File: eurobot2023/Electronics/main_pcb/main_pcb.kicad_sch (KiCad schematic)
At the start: 4 parts, among them J1 PI40HAT, J2 Conn_01x03, Q1 BSH108,215, U1 PCA9517AD

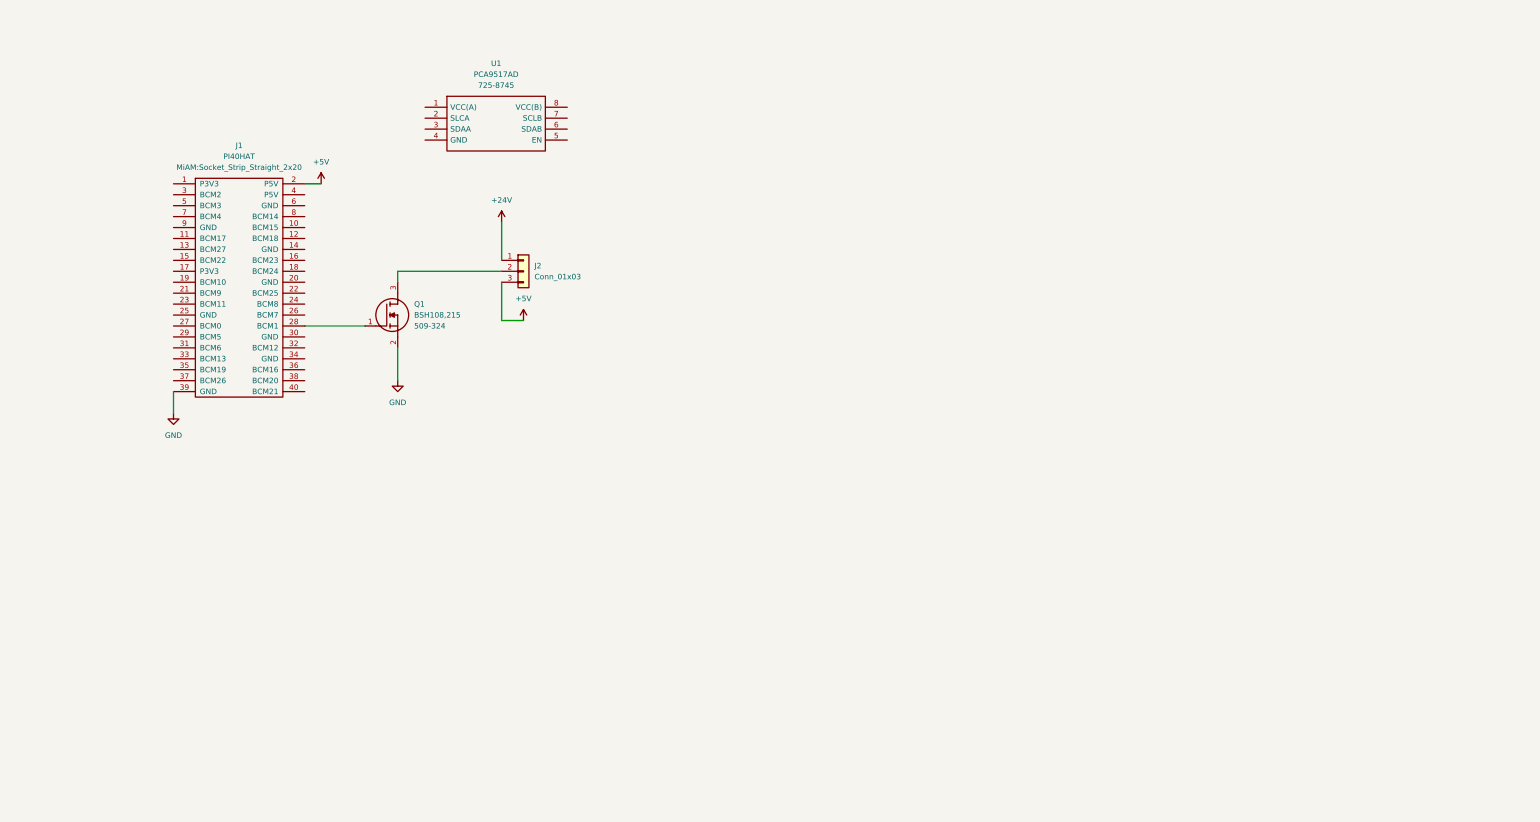
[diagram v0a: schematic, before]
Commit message: Electronics: partial draft of PCB.
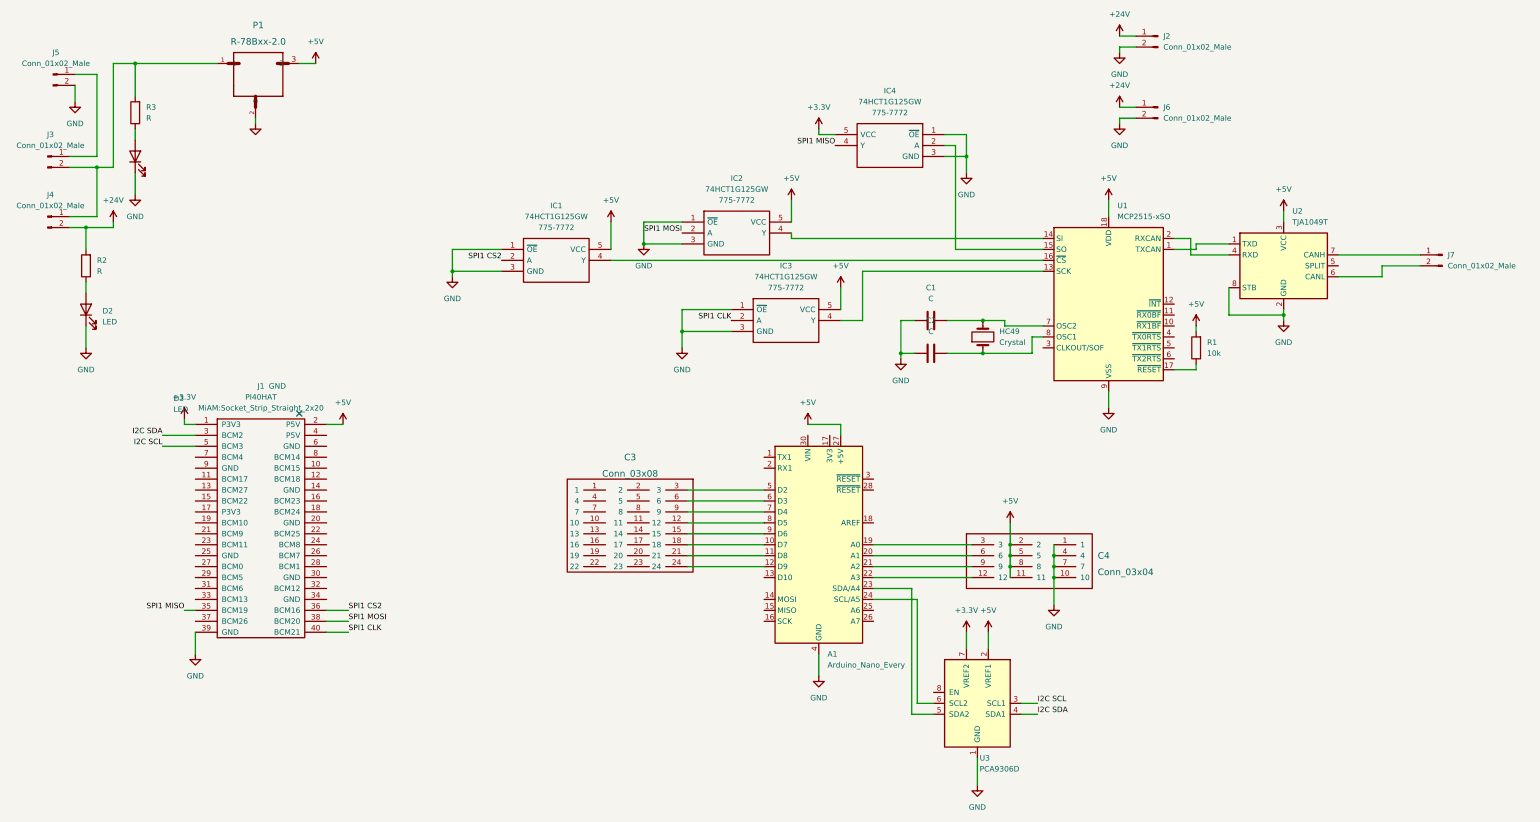
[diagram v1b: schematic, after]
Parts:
- removed J2: Conn_01x03, symbol Connector_Generic:Conn_01x03
- removed Q1: BSH108,215, SOT95P230X110-3N, symbol MiAM:BSH108,215
- removed U1: PCA9517AD, SOIC127P600X175-8N, symbol MiAM:PCA9517AD
- added A1: Arduino_Nano_Every, Module:Arduino_Nano, symbol MCU_Module:Arduino_Nano_Every
- added C1, C2: C, Capacitor_THT:C_Rect_L10.0mm_W2.5mm_P7.50mm_MKS4, symbol Device:C
- added C3: Conn_03x08, MiAM:Pin_Header_Straight_3x08_Pitch2.54mm, symbol MiAM:Conn_03x08
- added C4: Conn_03x04, MiAM:Pin_Header_Straight_3x04_Pitch2.54mm, symbol MiAM:Conn_03x04
- added D2, D3: LED, LED_THT:LED_D3.0mm, symbol Device:LED
- added HC49: Crystal, Crystal:Crystal_HC49-4H_Vertical, symbol Device:Crystal
- added IC1, IC2, IC3, IC4: 74HCT1G125GW, SOT65P210X110-5N, symbol MiAM:74HCT1G125GW
- added J2, J3, J4, J5, J6: Conn_01x02_Male, MiAM:XT30PWF, symbol Connector:Conn_01x02_Male
- added J7: Conn_01x02_Male, Connector_PinHeader_2.54mm:PinHeader_1x02_P2.54mm_Vertical, symbol Connector:Conn_01x02_Male
- added P1: R-78Bxx-2.0, MiAM:CONV_R-78Bxx-2.0, symbol MiAM:R-78Bxx-2.0
- added R1: 10k, Resistor_THT:R_Axial_DIN0309_L9.0mm_D3.2mm_P12.70mm_Horizontal, symbol Device:R
- added R2, R3: R, Resistor_THT:R_Axial_DIN0309_L9.0mm_D3.2mm_P12.70mm_Horizontal, symbol Device:R
- added U1: MCP2515-xSO, Package_SO:SOIC-18W_7.5x11.6mm_P1.27mm, symbol Interface_CAN_LIN:MCP2515-xSO
- added U2: TJA1049T, Package_SO:SOIC-8_3.9x4.9mm_P1.27mm, symbol Interface_CAN_LIN:TJA1049T
- added U3: PCA9306D, Package_SO:SO-8_3.9x4.9mm_P1.27mm, symbol Interface:PCA9306D
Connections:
- net +24V: now also J2.1 (Pin_1), J4.2 (Pin_2), J6.1 (Pin_1), R2.2
- net +5V: now also A1.27 (+5V), C4.11, C4.2, C4.5, C4.8, IC1.5 (VCC), IC2.5 (VCC), IC3.5 (VCC), P1.3, R1.2, U1.18 (VDD), U2.3 (VCC), U3.2 (VREF1)
- net GND: now also A1.29 (GND), A1.4 (GND), C1.1, C2.1, C4.1, C4.10, C4.4, C4.7, D2.1 (K), D3.1 (K), IC1.1 (~{OE}), IC1.3 (GND), IC2.1 (~{OE}), IC2.3 (GND), IC3.1 (~{OE}), IC3.3 (GND), IC4.1 (~{OE}), IC4.3 (GND), J2.2 (Pin_2), J5.2 (Pin_2), J6.2 (Pin_2), P1.2, U1.9 (VSS), U2.2 (GND), U2.8 (STB), U3.1 (GND)
- net +3.3V: now reaches J1.1 (P3V3)
- net +3.3V: now also IC4.5 (VCC), U3.7 (VREF2)
- net I2C SDA: now reaches J1.3 (BCM2)
- net I2C SDA: now also U3.4 (SDA1)
- net SPI1 MISO: now reaches J1.35 (BCM19)
- net SPI1 MISO: now also IC4.4 (Y)
- net SPI1 CS2: now reaches J1.36 (BCM16)
- net SPI1 CS2: now also IC1.2 (A)
- net SPI1 MOSI: now reaches J1.38 (BCM20)
- net SPI1 MOSI: now also IC2.2 (A)
- net SPI1 CLK: now reaches J1.40 (BCM21)
- net SPI1 CLK: now also IC3.2 (A)
- net I2C SCL: now reaches J1.5 (BCM3)
- net I2C SCL: now also U3.3 (SCL1)
- new net: J3.1 (Pin_1), J5.1 (Pin_1)
- new net: A1.22 (A3), C4.12
- new net: A1.19 (A0), C4.3
- new net: A1.20 (A1), C4.6
- new net: A1.21 (A2), C4.9
- new net: IC3.4 (Y), U1.13 (SCK)
- new net: J3.2 (Pin_2), J4.1 (Pin_1), P1.1, R3.2
- new net: IC2.4 (Y), U1.14 (SI)
- new net: U1.1 (TXCAN), U2.1 (TXD)
- new net: U1.2 (RXCAN), U2.4 (RXD)
- new net: J7.2 (Pin_2), U2.6 (CANL)
- new net: J7.1 (Pin_1), U2.7 (CANH)
- new net: A1.10 (D7), C3.18
- new net: A1.11 (D8), C3.21
- new net: A1.12 (D9), C3.24
- new net: A1.23 (SDA/A4), U3.5 (SDA2)
- new net: A1.24 (SCL/A5), U3.6 (SCL2)
- new net: A1.5 (D2), C3.3
- new net: A1.6 (D3), C3.6
- new net: A1.7 (D4), C3.9
- new net: A1.8 (D5), C3.12
- new net: A1.9 (D6), C3.15
- new net: IC4.2 (A), U1.15 (SO)
- new net: C2.2, HC49.1, U1.8 (OSC1)
- new net: C1.2, HC49.2, U1.7 (OSC2)
- new net: D2.2 (A), R2.1
- new net: IC1.4 (Y), U1.16 (~{CS})
- new net: D3.2 (A), R3.1
- new net: R1.1, U1.17 (~{RESET})
- no-connect marks 0 -> 1
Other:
- moved on the sheet: J1

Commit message: [eurobot2023/Electronics] Continue schematic
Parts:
- removed IC1, IC2, IC4: 74HCT1G125GW, SOT65P210X110-5N, symbol MiAM:74HCT1G125GW
- added IC1: 74HCT541D,652, SOIC127P1032X265-20N, symbol MiAM:74HCT541D,652
- added IC2: SN74LVC126ADR, SOIC127P600X175-14N, symbol MiAM:SN74LVC126ADR
- added J10: Conn_01x02_Male, Connector_PinHeader_2.54mm:PinHeader_1x02_P2.54mm_Vertical, symbol Connector:Conn_01x02_Male
- added J8: Conn_01x03_Male, Connector_PinHeader_2.54mm:PinHeader_1x03_P2.54mm_Vertical, symbol Connector:Conn_01x03_Male
- added J9: 22-03-5035, SHDR3W60P0X250_1X3_990X490X590P, symbol MiAM:22-03-5035
- added R4, R5, R6: 10k, Resistor_THT:R_Axial_DIN0309_L9.0mm_D3.2mm_P12.70mm_Horizontal, symbol Device:R
- added U4: Pololu_MAX14870, MiAM:PololuMAX14870, symbol MiAM:Pololu_MAX14870
- J1: footprint MiAM:Socket_Strip_Straight_2x20 -> MiAM:MODULE_RASPBERRY_PI_B+
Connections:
- net +24V: now also J8.3 (Pin_3)
- net +3.3V: now also IC2.1 (1OE), IC2.10 (3OE), IC2.13 (4OE), IC2.14 (VCC), R4.2, R5.2
- net +5V: now also J1.4 (P5V), IC1.20 (VCC), R6.2
- net GND: now also IC1.1 (~{OE1}), IC1.10 (GND), IC1.19 (~{OE2}), IC2.7 (GND), J9.3, U4.4 (nEnable), U4.5 (GND); no longer IC3.1 (~{OE})
- net SPI1 CLK: now also IC1.6 (A4); no longer IC3.2 (A)
- net SPI1 CS2: now also IC1.4 (A2)
- net SPI1 MISO: now also IC2.3 (1Y)
- net SPI1 MOSI: now also IC1.5 (A3)
- net SPI1 CLK_5: now reaches U1.13 (SCK)
- net SPI1 CLK_5: now also IC1.14 (Y4); no longer IC3.4 (Y)
- net SPI1 MOSI_5: now reaches U1.14 (SI)
- net SPI1 MOSI_5: now also IC1.15 (Y3)
- net SPI1 MISO_5: now reaches U1.15 (SO)
- net SPI1 MISO_5: now also IC2.2 (1A)
- net SPI1_CS0_5: now reaches U1.16 (~{CS})
- net SPI1_CS0_5: now also IC1.18 (Y0)
- net UART_RX: now reaches J1.10 (BCM15)
- net UART_RX: now also IC2.6 (2Y)
- net SPI1_CS0: now reaches J1.11 (BCM17)
- net SPI1_CS0: now also IC1.2 (A0)
- net SPI1_CS1: now reaches J1.12 (BCM18)
- net SPI1_CS1: now also IC1.3 (A1)
- net Servo RX: now reaches J1.16 (BCM23)
- net Servo RX: now also IC3.1 (~{OE}), IC2.4 (2OE), R5.1
- net UART_TX: now reaches J1.8 (BCM14)
- net UART_TX: now also IC1.7 (A5)
- new net: J10.1 (Pin_1), U4.7 (M1)
- new net: J10.2 (Pin_2), U4.8 (M2)
- new net: J8.2 (Pin_2), U4.9 (Vin)
- new net +7.5V: J8.1 (Pin_1), J9.2
- new net SPI1 CS2_5: IC1.16 (Y2)
- new net SPI1_CS1_5: IC1.17 (Y1)
- new net UART_RX_5: IC2.5 (2A), IC3.4 (Y), J9.1, R4.1, R6.1
- new net UART_TX_5: IC1.13 (Y5), IC3.2 (A)
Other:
- note added: "Arduino Nano"
- note added: "CAN & Motors"
- note added: "Logic level shifting"
- note added: "Power distribution"
- note added: "Pump & other DC motor"
- note added: "RC servos"
- note added: "Smart Servos"
- note added: "[TODO] - Encoders - Transistor for power switch - Access to I2C port - Access to second SPI port"
- moved on the sheet: A1, C1, C2, C3, C4, HC49, J1, J2, J6, J7, R1, U1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

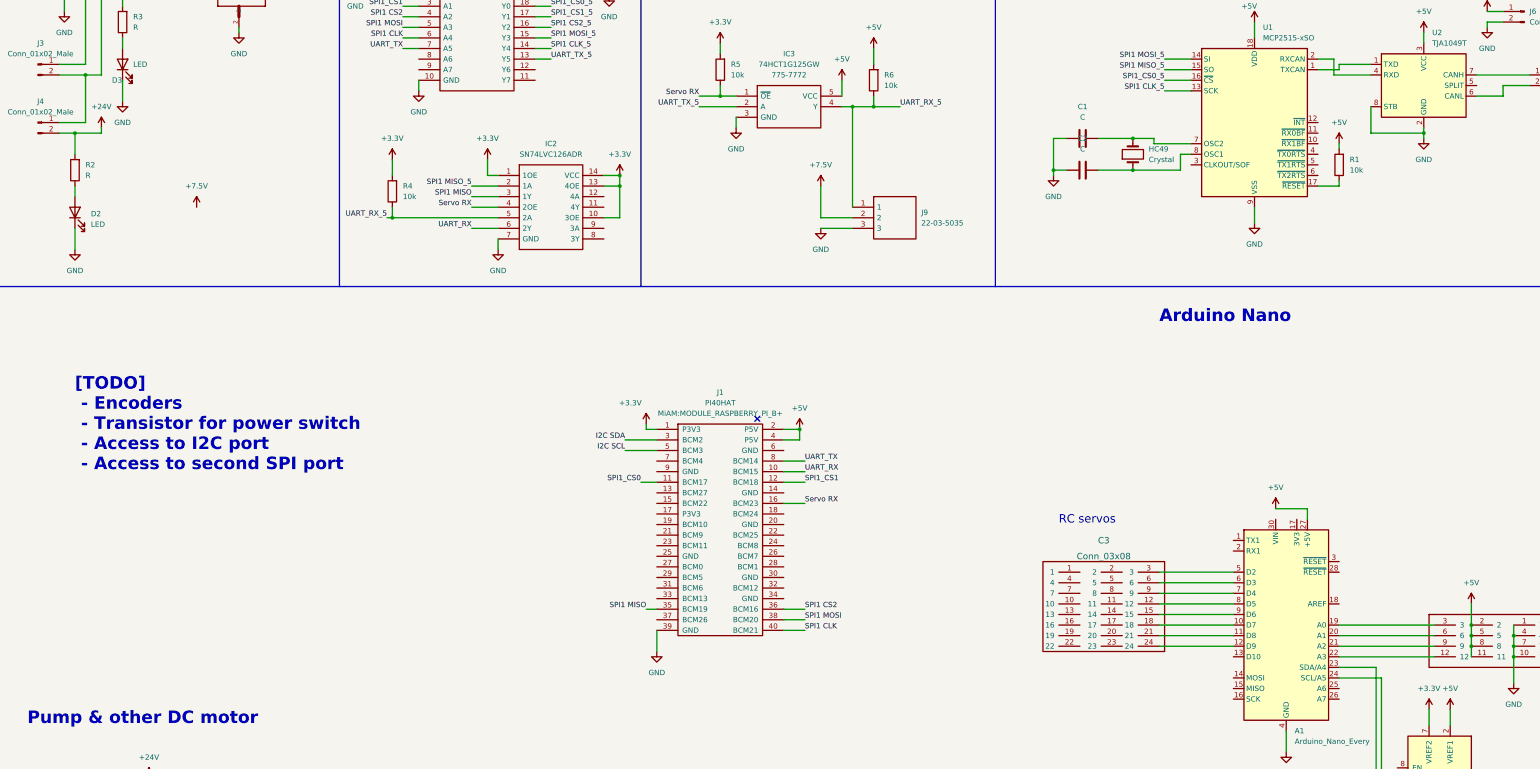
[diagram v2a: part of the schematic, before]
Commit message: [miam_utils] Add driver for the AS5045 magnetic encoder.
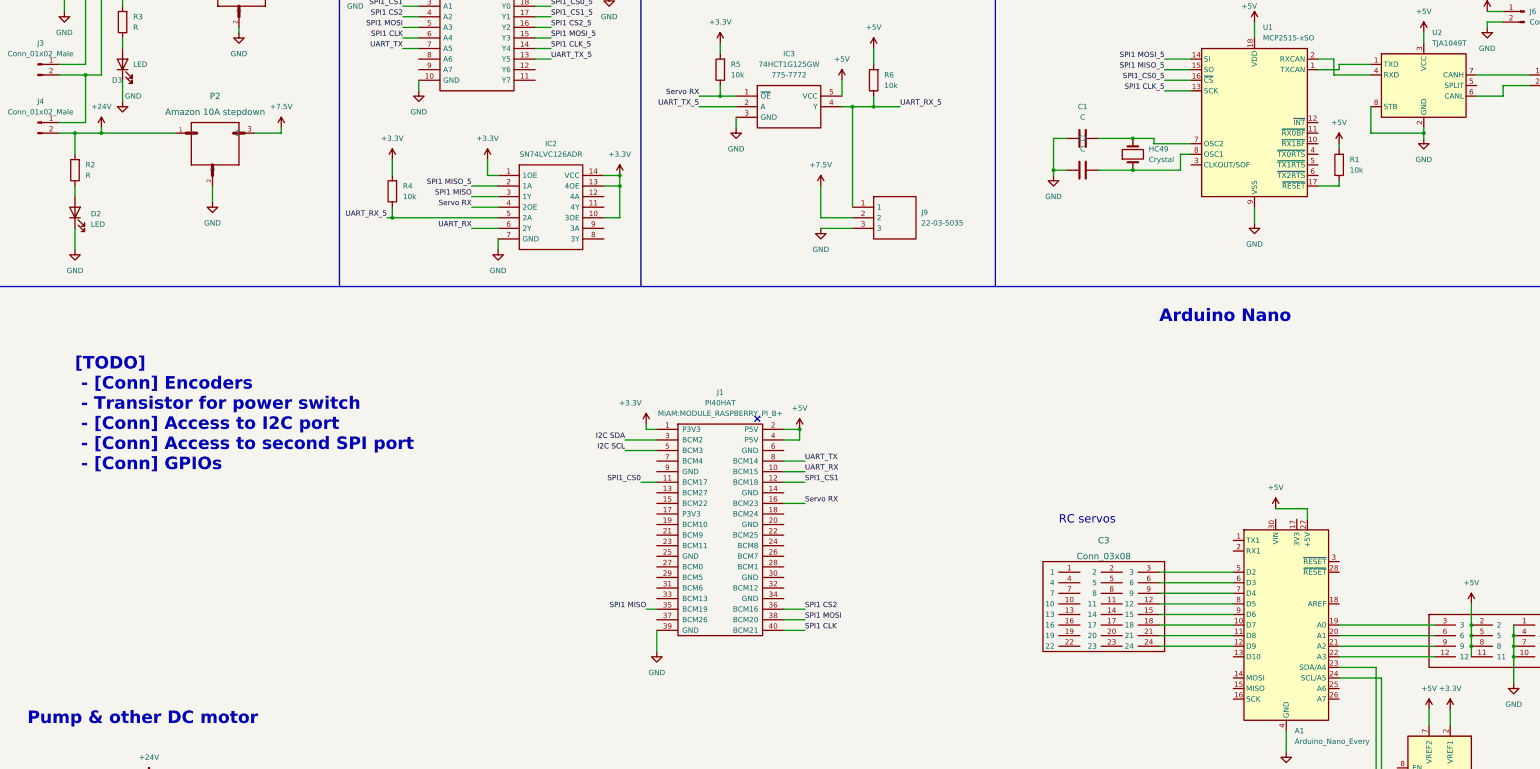
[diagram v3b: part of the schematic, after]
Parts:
- added P2: Amazon 10A stepdown, MiAM:StepDown10A, symbol MiAM:Amazon 10A stepdown
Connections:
- net +24V: now also P2.1
- net +3.3V: now also U3.2 (VREF1); no longer U3.7 (VREF2)
- net +5V: now also U3.7 (VREF2); no longer U3.2 (VREF1)
- net +7.5V: now also P2.3
- net GND: now also P2.2
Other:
- note added: "[TODO] - [Conn] Encoders - Transistor for power switch - [Conn] Access to I2C port - [Conn] Access to second SPI port - [Conn] GPIOs"
- note removed: "[TODO] - Encoders - Transistor for power switch - Access to I2C port - Access to second SPI port"

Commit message: PDB update.
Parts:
- added J11: MagneticEncoder, MiAM:52746-0671, symbol MiAM:MagneticEncoder
- J2, J3, J4, J5, J6: footprint MiAM:XT30PWF -> MiAM:XT30UM; RS number 180-5359 -> (none)
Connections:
- net +24V: now also J5.1 (Pin_1); no longer J2.1 (Pin_1)
- net +3.3V: now also J11.6 (Vcc)
- net GND: now also J3.2 (Pin_2), J11.1 (GND); no longer J2.2 (Pin_2)
- net SPI1 CLK: now also J11.4 (CLK)
- net SPI1 MISO: now also J11.3 (MISO)
- net SPI1 MOSI: now also J11.5 (MOSI)
- net SPI1_CS1: now also J11.2 (CS)
- net at J3.1 (Pin_1): now also J2.1 (Pin_1); no longer J5.1 (Pin_1)
- net at J4.1 (Pin_1), P1.1, R3.2: now also J2.2 (Pin_2); no longer J3.2 (Pin_2)

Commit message: Update pcb
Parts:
- removed A1: Arduino_Nano_Every, Module:Arduino_Nano, symbol MCU_Module:Arduino_Nano_Every
- removed J8: Conn_01x03_Male, Connector_PinHeader_2.54mm:PinHeader_1x03_P2.54mm_Vertical, symbol Connector:Conn_01x03_Male
- added J12: Conn_01x07_Male, Connector_PinHeader_2.54mm:PinHeader_1x07_P2.54mm_Vertical, symbol Connector:Conn_01x07_Male
- added J13: MagneticEncoder, MiAM:52746-0671, symbol MiAM:MagneticEncoder
- added J14: Conn_01x03_Male, Connector_PinHeader_2.54mm:PinHeader_1x03_P2.54mm_Vertical, symbol Connector:Conn_01x03_Male
- added J15: Conn_01x02_Male, Connector_PinHeader_2.54mm:PinHeader_1x02_P2.54mm_Vertical, symbol Connector:Conn_01x02_Male
- added U5: PCA9685PW, Package_SO:TSSOP-28_4.4x9.7mm_P0.65mm, symbol Driver_LED:PCA9685PW
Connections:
- net +3.3V: now also C4.11, C4.2, C4.5, C4.8, J12.1 (Pin_1), J13.6 (Vcc)
- net +5V: now also J14.1 (Pin_1), U5.2 (A1), U5.28 (VDD); no longer C4.11, C4.2, C4.5, C4.8
- net +7.5V: now also C3.11, C3.14, C3.17, C3.2, C3.20, C3.23, C3.5, C3.8, U4.9 (Vin)
- net GND: now also C3.1, C3.10, C3.13, C3.16, C3.19, C3.22, C3.4, C3.7, J12.2 (Pin_2), J13.1 (GND), J14.3 (Pin_3), U5.14 (VSS), U5.23 (~{OE}), U5.24 (A5), U5.25 (EXTCLK), U5.3 (A2), U5.4 (A3), U5.5 (A4)
- net I2C SCL: now also J12.3 (Pin_3)
- net I2C SDA: now also J12.4 (Pin_4)
- net SPI1 CLK: now also J1.23 (BCM11), J13.4 (CLK); no longer J1.40 (BCM21)
- net SPI1 CS2: no longer J1.36 (BCM16)
- net SPI1 MISO: now also J1.21 (BCM9), J13.3 (MISO); no longer J1.35 (BCM19)
- net SPI1 MOSI: now also J1.19 (BCM10), J13.5 (MOSI); no longer J1.38 (BCM20)
- net SPI1_CS0: now also J1.24 (BCM8); no longer J1.11 (BCM17)
- net SPI1_CS1: now also J1.26 (BCM7), J13.2 (CS); no longer J1.12 (BCM18)
- net Servo RX: now also J1.12 (BCM18); no longer J1.16 (BCM23)
- net GPIO 23: now reaches C4.12
- net GPIO 23: now also J1.16 (BCM23)
- net GPIO 20: now reaches C4.3
- net GPIO 20: now also J1.38 (BCM20)
- net GPIO 21: now reaches C4.6
- net GPIO 21: now also J1.40 (BCM21)
- net GPIO 22: now reaches C4.9
- net GPIO 22: now also J1.15 (BCM22)
- net at J7.2 (Pin_2), U2.6 (CANL): now also J15.2 (Pin_2)
- net at J7.1 (Pin_1), U2.7 (CANH): now also J15.1 (Pin_1)
- net at C3.18: now also U5.11 (LED5)
- net at C3.21: now also U5.12 (LED6)
- net at C3.24: now also U5.13 (LED7)
- net at U3.5 (SDA2): now also U5.27 (SDA)
- net at U3.6 (SCL2): now also U5.26 (SCL)
- net at C3.3: now also U5.6 (LED0)
- net at C3.6: now also U5.7 (LED1)
- net at C3.9: now also U5.8 (LED2)
- net at C3.12: now also U5.9 (LED3)
- net at C3.15: now also U5.10 (LED4)
- net GPIO 5: now reaches J1.29 (BCM5)
- net GPIO 5: now also J12.6 (Pin_6)
- net GPIO 6: now reaches J1.31 (BCM6)
- net GPIO 6: now also J12.7 (Pin_7)
- net GPIO 12: now reaches J1.32 (BCM12)
- net GPIO 12: now also U4.1 (PWM)
- net GPIO 4: now reaches J1.7 (BCM4)
- net GPIO 4: now also J12.5 (Pin_5)
- net GPIO 16: now reaches U4.2 (DIR)
- net GPIO 16: now also J1.36 (BCM16)
- new net A0: J14.2 (Pin_2), U5.1 (A0)
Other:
- note added: "GPIO"
- note added: "I2C"
- note added: "Servo driver"
- note added: "[TODO] - [Conn] Encoders - Transistor for power switch"
- note removed: "Arduino Nano"
- note removed: "[TODO] - [Conn] Encoders - Transistor for power switch - [Conn] Access to I2C port - [Conn] Access to second SPI port - [Conn] GPIOs"
- moved on the sheet: J1, U3
